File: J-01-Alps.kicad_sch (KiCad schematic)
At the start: 17 parts, among them SW1 SW_Push, U1 ATmega32U4-MU, U4 PRTR5V0U2X, Y1 16MHz

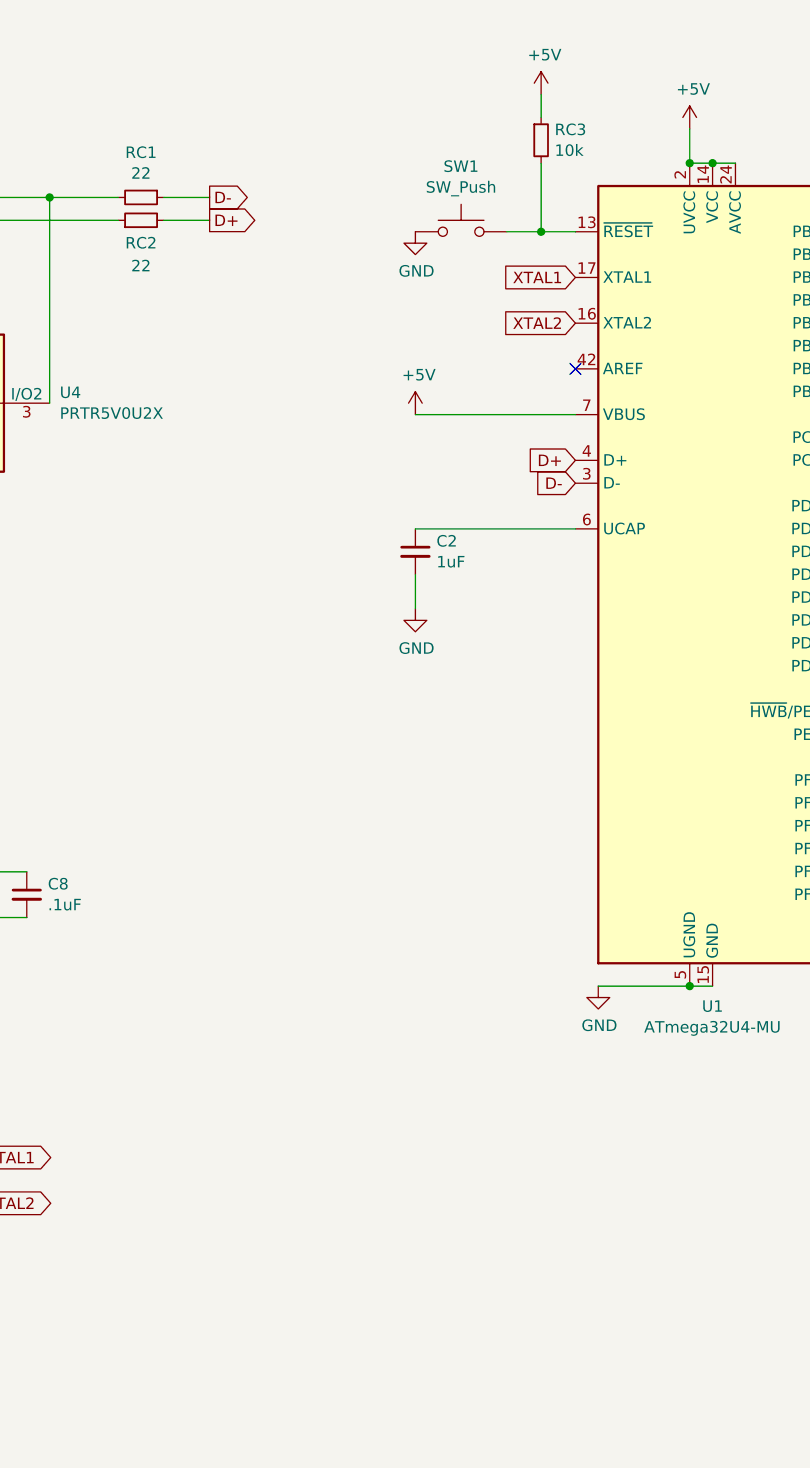
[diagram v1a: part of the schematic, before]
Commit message: Footprint cleanup, add AVR-ISP header footprint
Some cleanup of the bottom row, ISO enter layout, and capslock footprints for more clearance. Addition of the AVR ISP header footprint and mapping to the MCU.
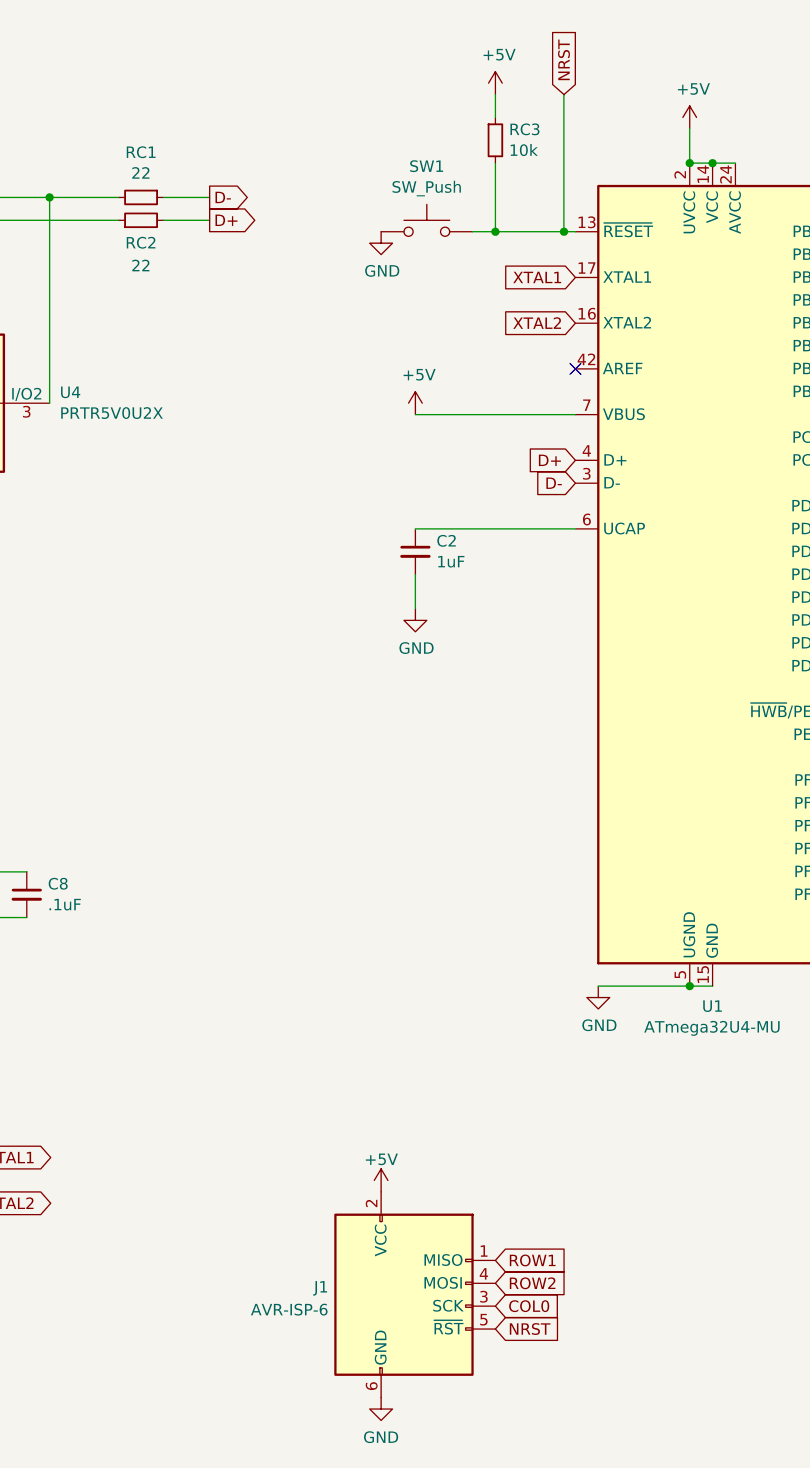
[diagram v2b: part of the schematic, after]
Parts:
- added J1: AVR-ISP-6, Connector_PinHeader_2.54mm:PinHeader_2x03_P2.54mm_Vertical, symbol Connector:AVR-ISP-6
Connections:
- net +5V: now also J1.2 (VCC)
- net COL0: now also J1.3 (SCK)
- net GND: now also J1.6 (GND)
- net ROW1: now also J1.1 (MISO)
- net ROW2: now also J1.4 (MOSI)
- net NRST: now reaches RC3.2, SW1.2, U1.13 (~{RESET})
- net NRST: now also J1.5 (~{RST})
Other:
- moved on the sheet: RC3, SW1
